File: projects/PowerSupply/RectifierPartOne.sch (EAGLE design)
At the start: 27 parts, among them K1 G2R2, K2 G2R2, X1 LINE-IN, X2 T1-PRI, X3 T1-SEC, X4 R1-OUT, X5 T2-PRI, X6 T2-SEC, X7 R2-OUT

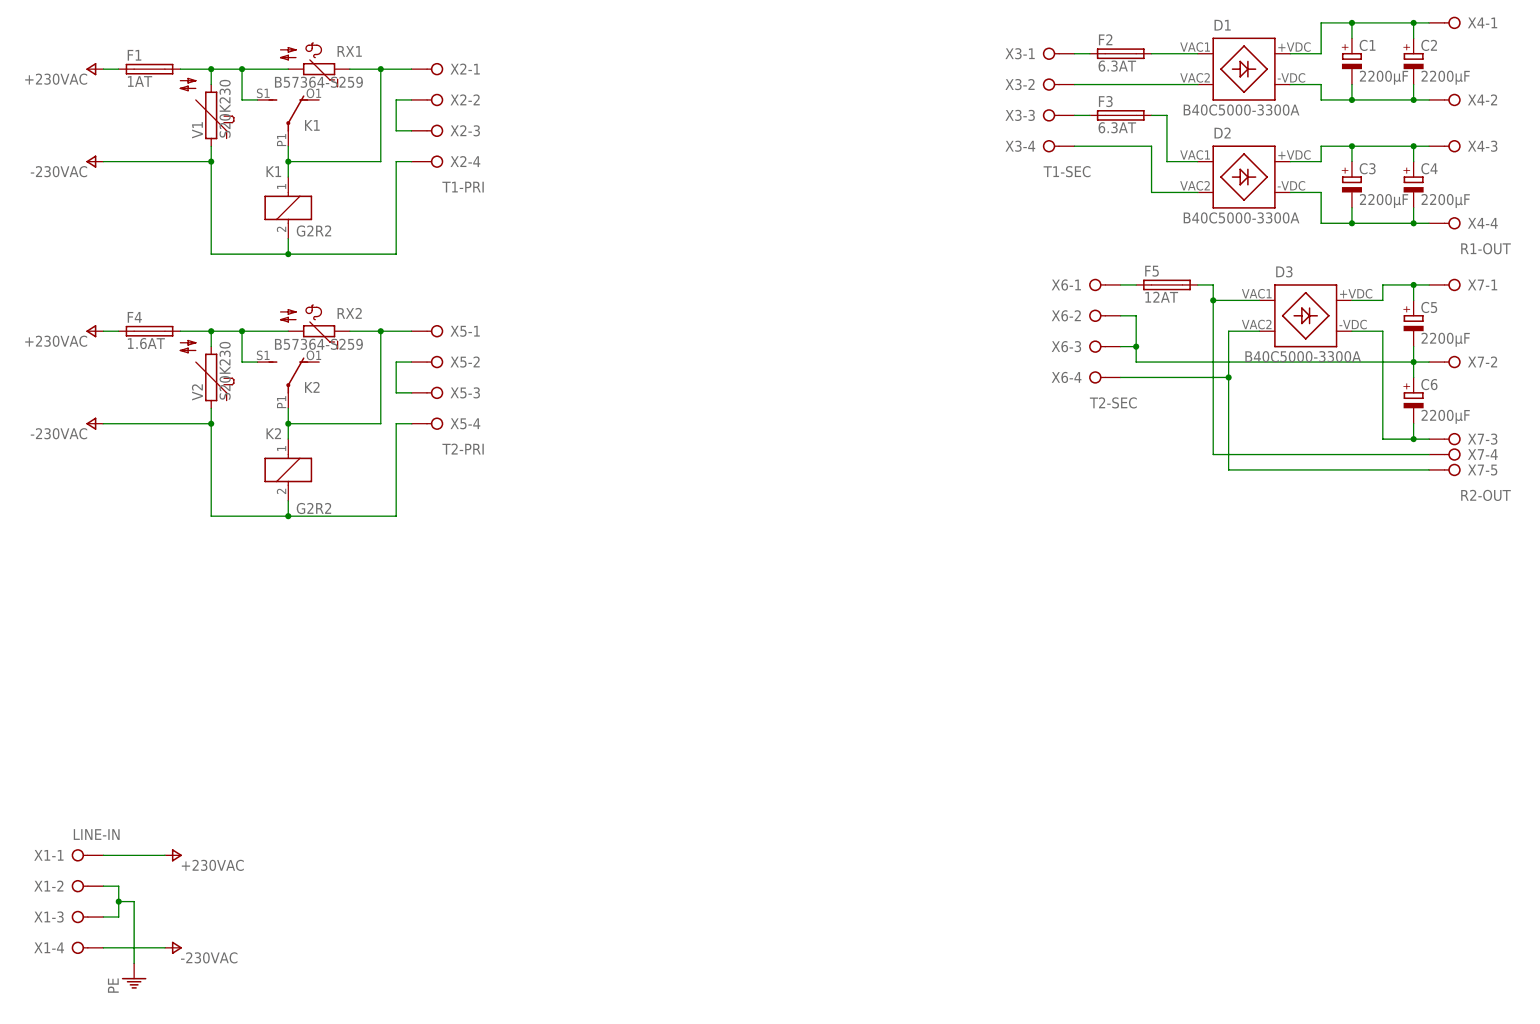
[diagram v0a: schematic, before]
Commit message: feat: rectifier part modified
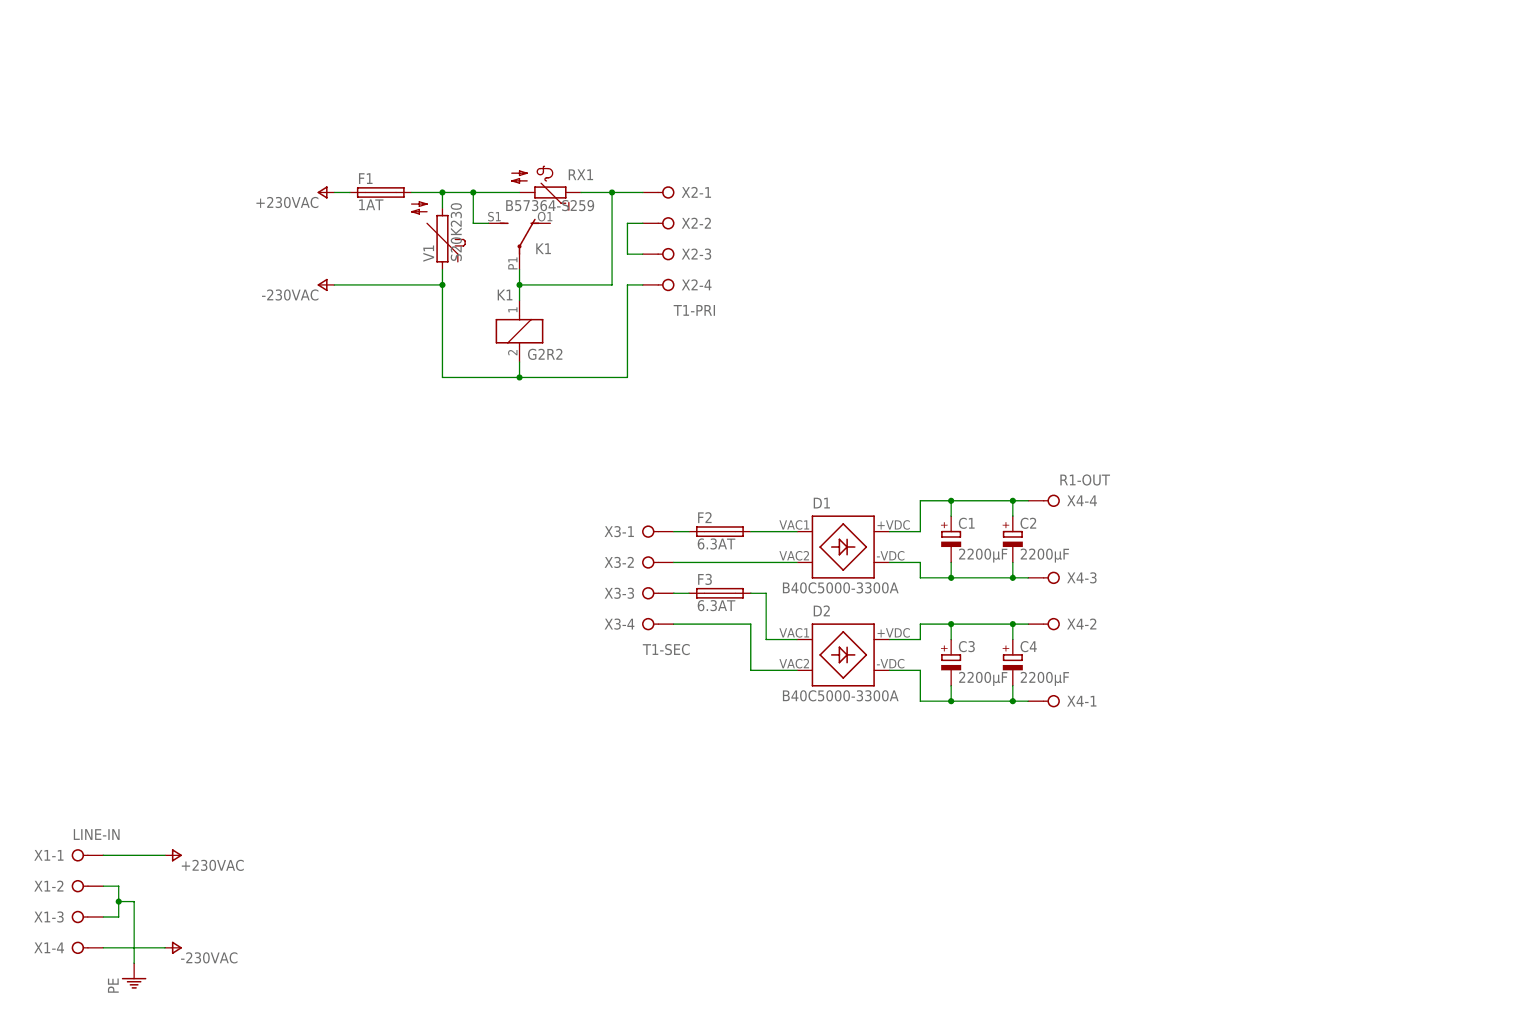
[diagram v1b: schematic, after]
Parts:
- removed C5, C6: 2200µF, rcl:CPOL-EUE7.5-16
- removed D3: B40C5000-3300A, bb84:B40C5000-3300A
- removed F4: 1.6AT, fuse:SH22,5A
- removed F5: 12AT, fuse:SH22,5A
- removed K2: G2R2, relay:G2R2
- removed RX2: B57364-S259, bb84:EPCB57364-S259
- removed V2: S20K230, varistor:S20K230
- removed X5: T2-PRI, con-wago-508:W237-04P
- removed X6: T2-SEC, con-wago-508:W237-04P
- removed X7: R2-OUT, con-wago-508:W237-05P
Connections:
- removed net N$11: F4.2, K22.S, RX2.2, V2.2
- removed net N$17: F5.1, X6-1.KL
- removed net N$18: D3.VAC1, F5.2, X7-4.KL
- removed net N$19: D3.VAC2, X6-4.KL, X7-5.KL
- removed net N$20: C5.+, D3.+VDC, X7-1.KL
- removed net N$21: C6.-, D3.-VDC, X7-3.KL
- removed net N$22: C5.-, C6.+, X6-2.KL, X6-3.KL, X7-2.KL
- removed net N$23: X5-2.KL, X5-3.KL
- removed net N$24: K21.1, K22.P, RX2.1, X5-1.KL
- net +230VAC: no longer F4.1
- net -230VAC: no longer K21.2, V2.1, X5-4.KL
- net N$4: now also X4-4.KL; no longer X4-1.KL
- net N$6: now also X4-2.KL; no longer X4-3.KL
- net N$7: now also X4-3.KL; no longer X4-2.KL
- net N$9: now also X4-1.KL; no longer X4-4.KL
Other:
- moved on the sheet: C1, C2, C3, C4, D1, D2, F1, F2, F3, K1, RX1, V1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

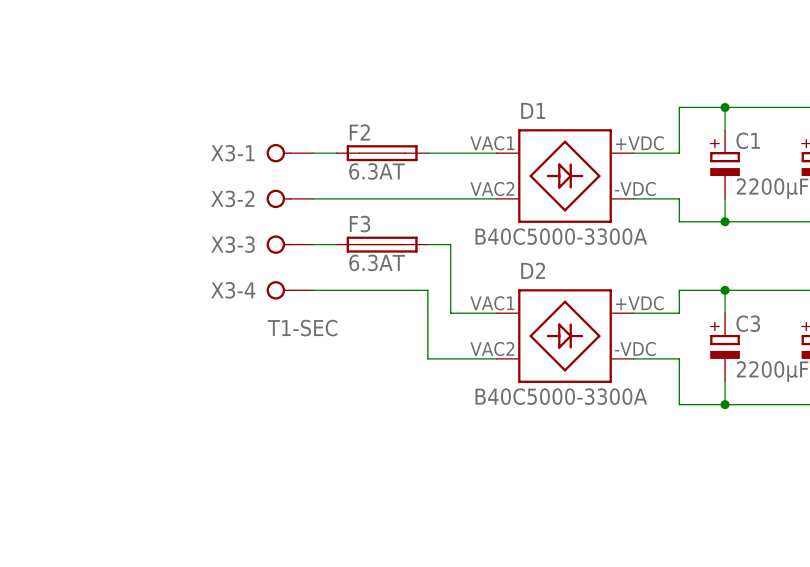
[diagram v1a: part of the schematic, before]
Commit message: feat: rectifier part one modified
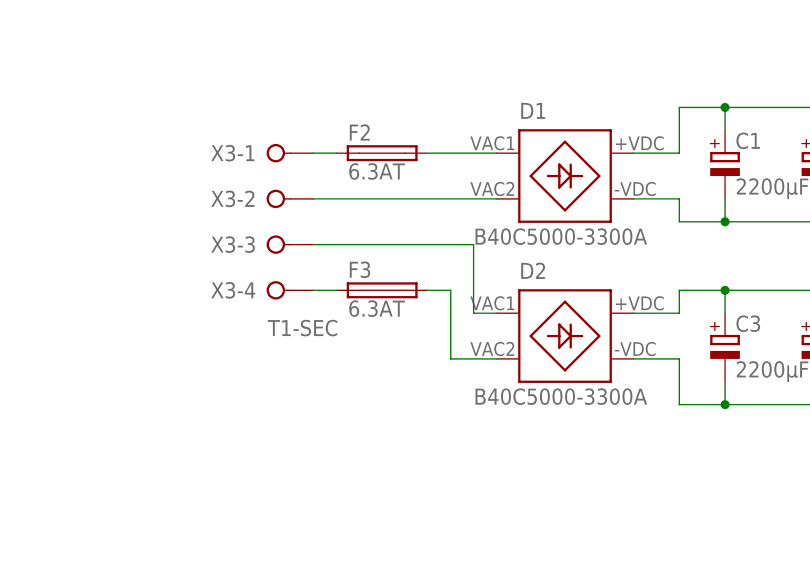
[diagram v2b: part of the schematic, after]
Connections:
- removed net N$13: F3.1, X3-3.KL
- removed net N$15: D2.VAC2, X3-4.KL
- new net N$11: D2.VAC2, F3.2
- new net N$12: F3.1, X3-4.KL
- net N$14: now also X3-3.KL; no longer F3.2
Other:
- moved on the sheet: F3
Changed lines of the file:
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@@
 <attribute name="NAME" x="13.97" y="18.669" size="1.778" layer="95" rot="R180"/>
 </instance>
-<instance part="F3" gate="1" x="121.92" y="76.2" smashed="yes">
-<attribute name="NAME" x="118.11" y="77.597" size="1.778" layer="95"/>
-<attribute name="VALUE" x="118.11" y="73.279" size="1.778" layer="96"/>
+<instance part="F3" gate="1" x="121.92" y="71.12" smashed="yes">
+<attribute name="NAME" x="118.11" y="72.517" size="1.778" layer="95"/>
+<attribute name="VALUE" x="118.11" y="68.199" size="1.778" layer="96"/>
 </instance>
 <instance part="X4" gate="-1" x="177.8" y="58.42" smashed="yes" rot="MR0">
@@
 </segment>
 </net>
-<net name="N$13" class="0">
-<segment>
+<net name="N$14" class="0">
+<segment>
+<pinref part="D2" gate="G$1" pin="VAC1"/>
+<wire x1="134.62" y1="68.58" x2="132.08" y2="68.58" width="0.1524" layer="91"/>
+<wire x1="132.08" y1="68.58" x2="132.08" y2="76.2" width="0.1524" layer="91"/>
 <pinref part="X3" gate="-3" pin="KL"/>
-<pinref part="F3" gate="1" pin="1"/>
-<wire x1="114.3" y1="76.2" x2="116.84" y2="76.2" width="0.1524" layer="91"/>
-</segment>
-</net>
-<net name="N$14" class="0">
-<segment>
-<pinref part="D2" gate="G$1" pin="VAC1"/>
-<wire x1="134.62" y1="68.58" x2="129.54" y2="68.58" width="0.1524" layer="91"/>
-<wire x1="129.54" y1="68.58" x2="129.54" y2="76.2" width="0.1524" layer="91"/>
-<pinref part="F3" gate="1" pin="2"/>
-<wire x1="129.54" y1="76.2" x2="127" y2="76.2" width="0.1524" layer="91"/>
-</segment>
-</net>
-<net name="N$15" class="0">
-<segment>
-<pinref part="D2" gate="G$1" pin="VAC2"/>
-<wire x1="134.62" y1="63.5" x2="127" y2="63.5" width="0.1524" layer="91"/>
-<wire x1="127" y1="63.5" x2="127" y2="71.12" width="0.1524" layer="91"/>
-<pinref part="X3" gate="-4" pin="KL"/>
-<wire x1="127" y1="71.12" x2="114.3" y2="71.12" width="0.1524" layer="91"/>
+<wire x1="114.3" y1="76.2" x2="132.08" y2="76.2" width="0.1524" layer="91"/>
 </segment>
 </net>
@@
 </segment>
 </net>
+<net name="N$12" class="0">
+<segment>
+<pinref part="F3" gate="1" pin="1"/>
+<pinref part="X3" gate="-4" pin="KL"/>
+<wire x1="116.84" y1="71.12" x2="114.3" y2="71.12" width="0.1524" layer="91"/>
+</segment>
+</net>
+<net name="N$11" class="0">
+<segment>
+<pinref part="F3" gate="1" pin="2"/>
+<wire x1="127" y1="71.12" x2="129.54" y2="71.12" width="0.1524" layer="91"/>
+<wire x1="129.54" y1="71.12" x2="129.54" y2="63.5" width="0.1524" layer="91"/>
+<pinref part="D2" gate="G$1" pin="VAC2"/>
+<wire x1="129.54" y1="63.5" x2="134.62" y2="63.5" width="0.1524" layer="91"/>
+</segment>
+</net>

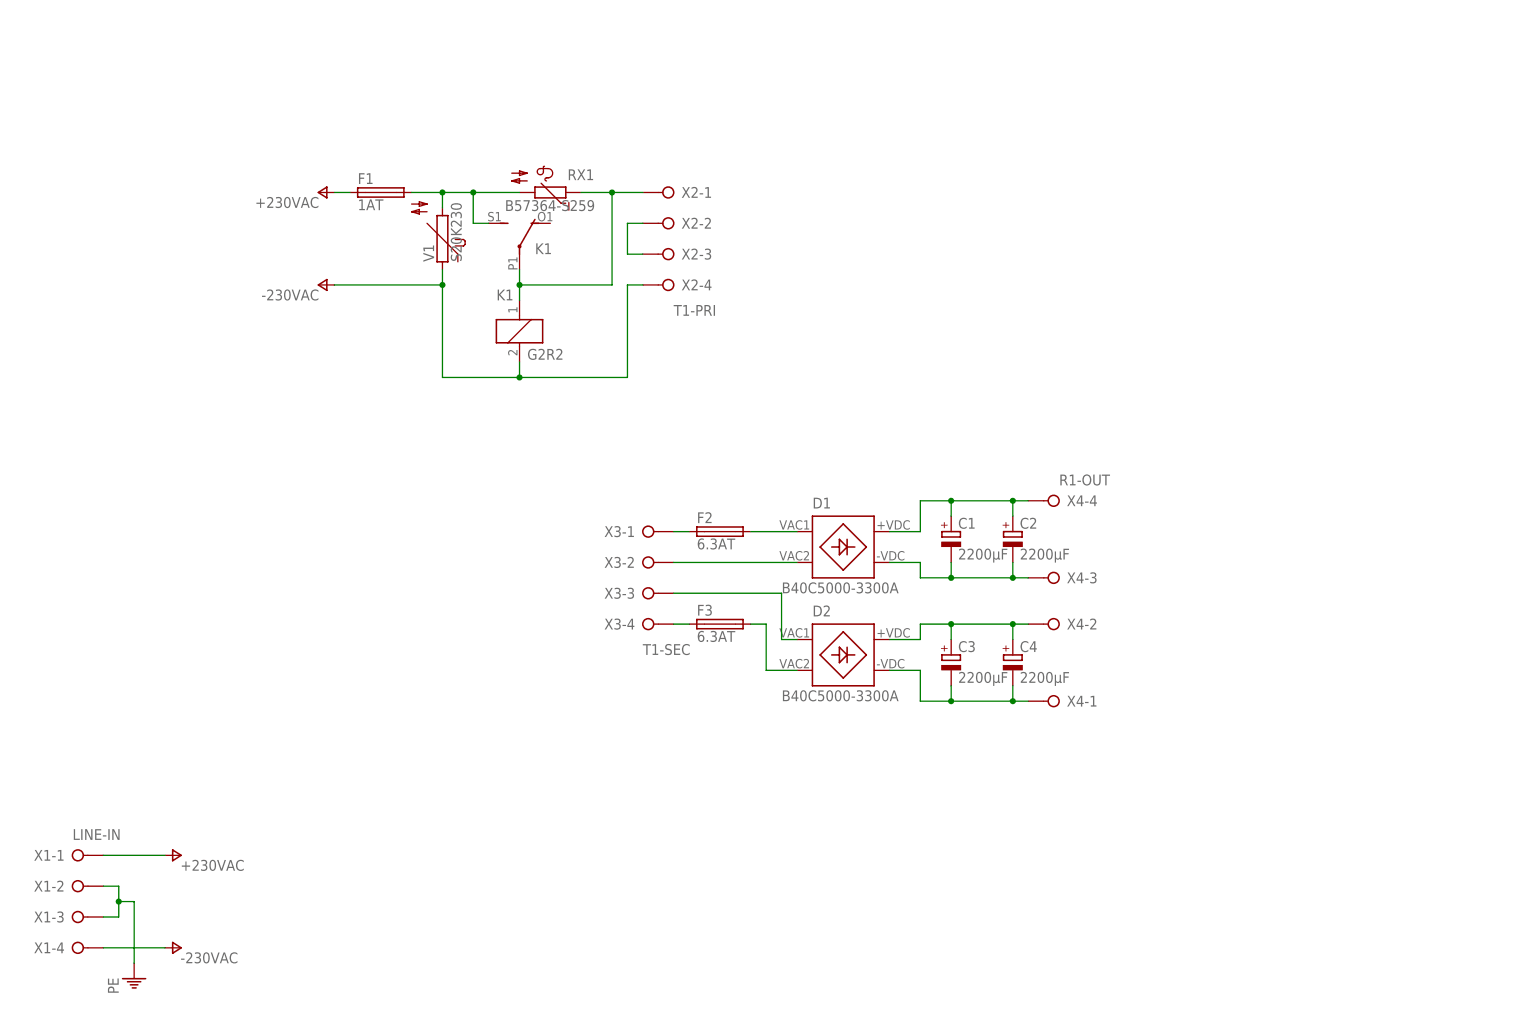
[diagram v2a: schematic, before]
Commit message: feat: rectifier part one modified
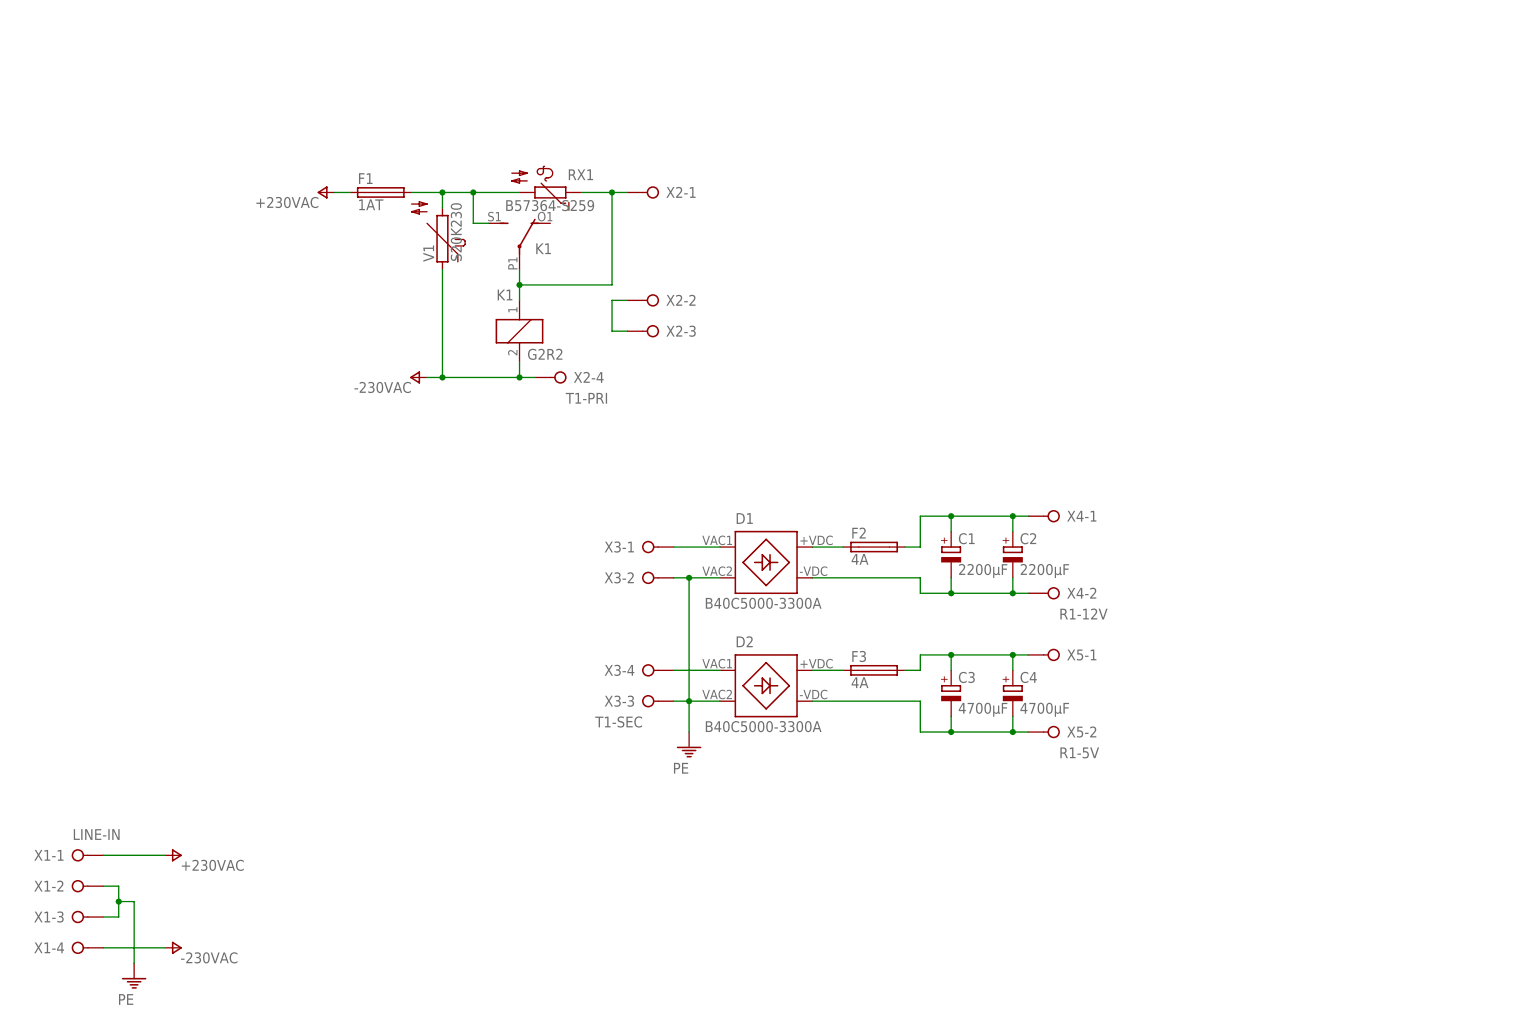
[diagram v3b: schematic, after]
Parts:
- added X5: R1-5V, con-wago-508:W237-02P
- C3, C4: value 2200µF -> 4700µF
- F2, F3: value 6.3AT -> 4A
- X4: value R1-OUT -> R1-12V; device con-wago-508:W237-04P -> con-wago-508:W237-02P
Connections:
- removed net N$12: F3.1, X3-4.KL
- removed net N$14: D2.VAC1, X3-3.KL
- net N$1: now also D1.VAC1, X3-1.KL; no longer D1.VAC2, X3-2.KL
- net N$10: now also D1.+VDC, F2.1; no longer D1.VAC1, F2.2
- net N$11: now also D2.+VDC, F3.1; no longer D2.VAC2, F3.2
- net N$4: now also F2.2, X4-1.KL; no longer D1.+VDC, X4-4.KL
- net N$6: now also F3.2, X5-1.KL; no longer D2.+VDC, X4-2.KL
- net N$7: now also X4-2.KL; no longer X4-3.KL
- net N$8: now also D2.VAC1, X3-4.KL; no longer F2.1, X3-1.KL
- net N$9: now also X5-2.KL; no longer X4-1.KL
- net PE: now also D1.VAC2, D2.VAC2, X3-2.KL, X3-3.KL
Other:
- moved on the sheet: C1, C2, C3, C4, D1, D2, F2, F3, X2-1, X2-2, X2-3, X2-4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
